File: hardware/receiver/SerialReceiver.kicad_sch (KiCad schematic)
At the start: 42 parts, among them J1 DATA, J2 CONTROL, J3 RX, J4 Clock select, J5 LED enable, J6 Mode select, Q1 2N7000, Q2 2N7000, SW1 SW_Push, U1 74HC132, U2 74HC191, U3 74HC191, U4 74HC595, U5 74HC74, U6 74LS244

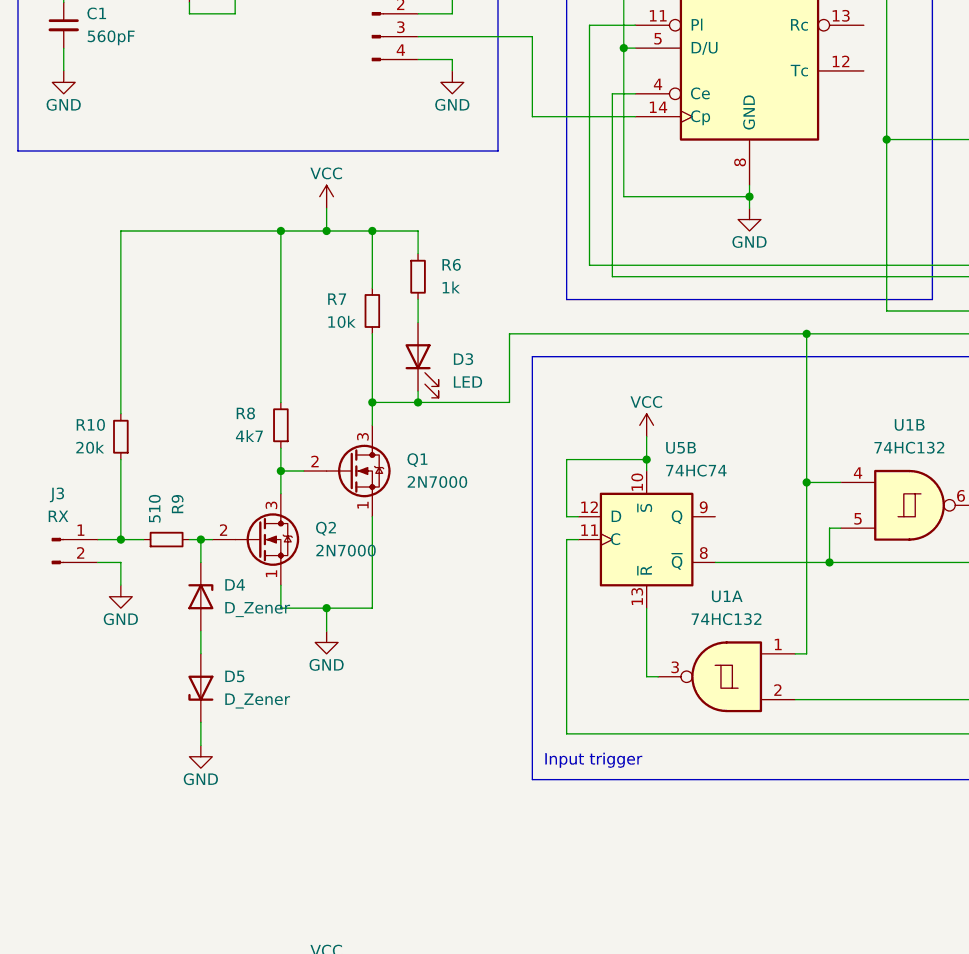
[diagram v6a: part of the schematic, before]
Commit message: The receiver's PCB is finished.
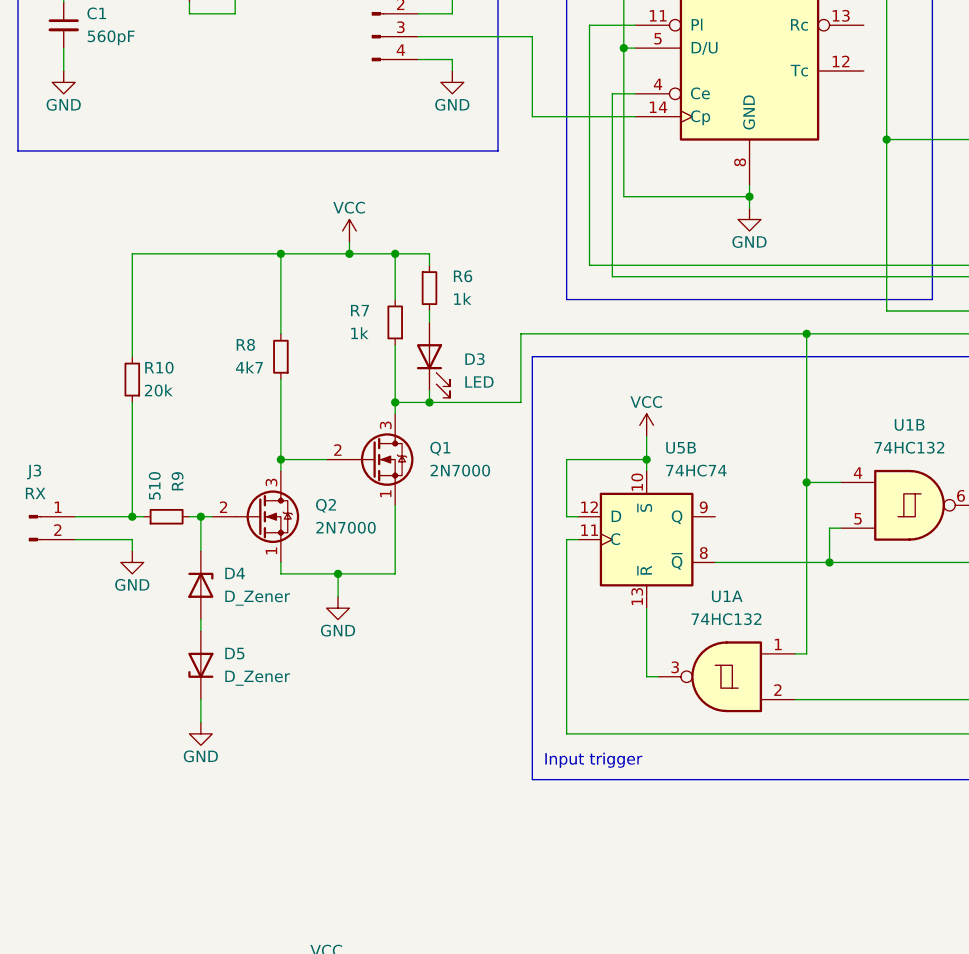
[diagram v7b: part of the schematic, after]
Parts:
- R7: value 10k -> 1k
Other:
- moved on the sheet: D3, D4, D5, J3, Q1, Q2, R10, R6, R7, R8, R9

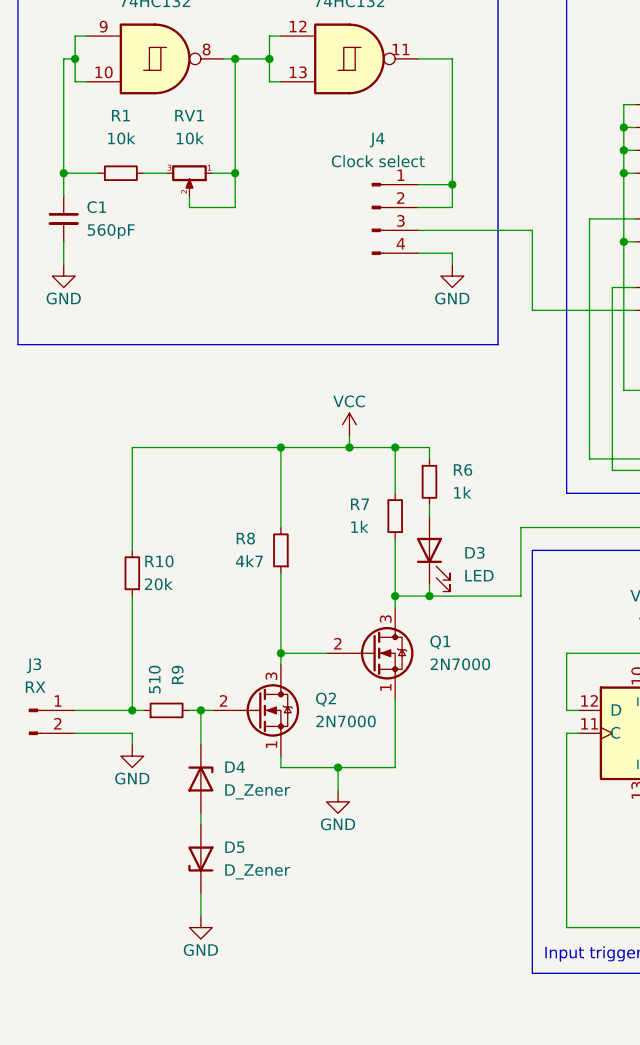
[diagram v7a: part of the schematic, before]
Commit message: The schematic and the PCB is finished.
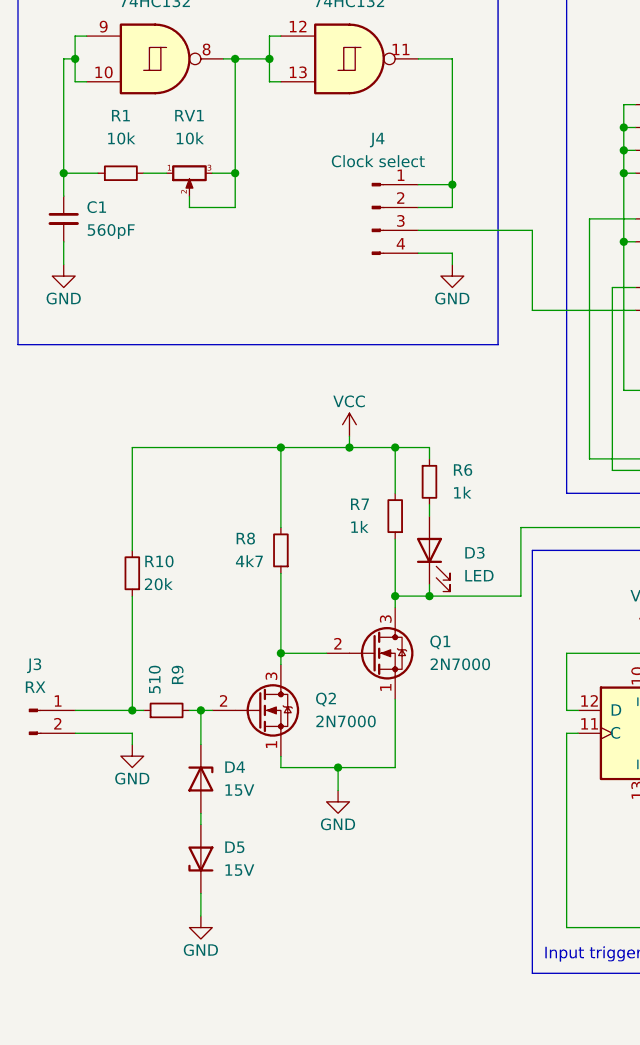
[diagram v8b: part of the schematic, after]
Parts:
- D4, D5: value D_Zener -> 15V
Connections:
- net at R1.2: now also RV1.1; no longer RV1.3
- net at RV1.2, U1.12, U1.13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: now also RV1.3; no longer RV1.1
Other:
- moved on the sheet: RV1
